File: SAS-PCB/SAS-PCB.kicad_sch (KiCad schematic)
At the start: 8 parts, among them J1 Conn_SMA_RF2-04A-T-00-50-G, J1-BMP280 Conn_01x06_Pin, J2 Conn_02x20_Odd_Even, J3-GPS Conn_01x04_Socket, J4-LCD1 Conn_01x04_Socket, J5-LCD2 Conn_01x04_Socket, J6-FAN1 Conn_01x02_Pin, J7-FAN2 Conn_01x02_Pin

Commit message: schematic done
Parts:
- removed J1: Conn_SMA_RF2-04A-T-00-50-G, CONN_RF2-04A-T-00-50-G_ADM, symbol SAS-librairie_symboles:Conn_SMA_RF2-04A-T-00-50-G
- removed J5-LCD2: Conn_01x04_Socket, symbol Connector:Conn_01x04_Socket
- removed J6-FAN1, J7-FAN2: Conn_01x02_Pin, symbol Connector:Conn_01x02_Pin
- added Bouton_1, Bouton_2, Bouton_3, Bouton_4, Bouton_5, Bouton_6, Fan_1, Fan_2, J5_Batt1, RFD900x1: 691137710002, SAS-Librarie-Empreinte:bornie_2position, symbol SAS-librairie_symboles:bornier_2position
- added J4-LCD2: Conn_01x04_Socket, SAS-Librarie-Empreinte:Conn_4_pos, symbol Connector:Conn_01x04_Socket
- added R1, R2, R3, R4, R5, R6, R7, R8: 1k, SAS-Librarie-Empreinte:Resistance, symbol Device:R
- J1-BMP280: footprint (none) -> SAS-Librarie-Empreinte:Conn_6_pos
- J2: footprint (none) -> Connector_PinSocket_2.54mm:PinSocket_2x20_P2.54mm_Vertical
- J3-GPS1: renamed from J3-GPS; footprint (none) -> SAS-Librarie-Empreinte:Conn_4_pos
- J4-LCD1: footprint (none) -> SAS-Librarie-Empreinte:Conn_4_pos
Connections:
- net +5V: now also J4-LCD1.2 (Pin_2), Fan_1.2 (5V), Fan_2.2 (5V), J4-LCD2.2 (Pin_2), J5_Batt1.2 (5V), RFD900x1.2 (5V)
- net GND: now also J1-BMP280.2 (Pin_2), J2.14 (Pin_14), J2.20 (Pin_20), J2.25 (Pin_25), J2.30 (Pin_30), J2.34 (Pin_34), J2.39 (Pin_39), J2.6 (Pin_6), J2.9 (Pin_9), J3-GPS1.4 (Pin_4), J4-LCD1.1 (Pin_1), Fan_1.1 (GND), Fan_2.1 (GND), J4-LCD2.1 (Pin_1), J5_Batt1.1 (GND), RFD900x1.1 (GND)
- net +3.3V: now reaches J3-GPS1.1 (Pin_1)
- net +3.3V: now also J1-BMP280.1 (Pin_1), J1-BMP280.5 (Pin_5), J1-BMP280.6 (Pin_6), J2.1 (Pin_1), J2.17 (Pin_17), Bouton_1.2 (5V), Bouton_2.2 (5V), Bouton_3.2 (5V), Bouton_4.2 (5V), Bouton_5.2 (5V), Bouton_6.2 (5V), R7.2, R8.2
- net TXD: now reaches J3-GPS1.2 (Pin_2)
- net TXD: now also J2.8 (Pin_8)
- net RXD: now reaches J3-GPS1.3 (Pin_3)
- net RXD: now also J2.10 (Pin_10)
- net Bouton_1: now reaches J2.27 (Pin_27)
- net Bouton_1: now also R1.2
- net Bouton_2: now reaches J2.29 (Pin_29)
- net Bouton_2: now also R2.2
- net SDA: now reaches J2.3 (Pin_3)
- net SDA: now also J1-BMP280.4 (Pin_4), J4-LCD1.3 (Pin_3), J4-LCD2.3 (Pin_3), R7.1
- net Bouton_3: now reaches J2.31 (Pin_31)
- net Bouton_3: now also R3.1
- net Bouton_4: now reaches J2.33 (Pin_33)
- net Bouton_4: now also R4.1
- net Bouton_5: now reaches J2.35 (Pin_35)
- net Bouton_5: now also R5.1
- net Bouton_6: now reaches J2.37 (Pin_37)
- net Bouton_6: now also R6.1
- net SCL: now reaches J2.5 (Pin_5)
- net SCL: now also J1-BMP280.3 (Pin_3), J4-LCD1.4 (Pin_4), J4-LCD2.4 (Pin_4), R8.1
- new net: Bouton_6.1 (GND), R6.2
- new net: Bouton_5.1 (GND), R5.2
- new net: Bouton_2.1 (GND), R2.1
- new net: Bouton_1.1 (GND), R1.1
- new net: Bouton_4.1 (GND), R4.2
- new net: Bouton_3.1 (GND), R3.2
- no-connect marks 0 -> 2
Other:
- moved on the sheet: J1-BMP280, J4-LCD1

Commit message: Rooting terminé
Reste à refaire les mounting holes et enlever les bouttes de cuivre trop mince.
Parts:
- removed Fan_1, Fan_2: 691137710002, SAS-Librarie-Empreinte:bornie_2position, symbol SAS-librairie_symboles:bornier_2position
- added J8-Fan1, J9-Fan2: Conn_01x04_Socket, SAS-Librarie-Empreinte:Conn_4_pos, symbol Connector:Conn_01x04_Socket
- J4-BMP280: renamed from J1-BMP280; footprint SAS-Librarie-Empreinte:Conn_6_pos -> SAS-Librarie-Empreinte:Header-BMP280
- J5-GPS1: renamed from J3-GPS1; footprint SAS-Librarie-Empreinte:Conn_4_pos -> SAS-Librarie-Empreinte:conn-GPS
- renumbered J5_Batt1 to J1_Batt1, J4-LCD1 to J2-LCD1, J4-LCD2 to J3-LCD2, J2 to J6-cable-plat1, RFD900x1 to J7-RFD900x1
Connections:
- net +5V: now also J8-Fan1.2 (Pin_2), J9-Fan2.2 (Pin_2)
- net GND: now also J8-Fan1.1 (Pin_1), J9-Fan2.1 (Pin_1)
- net Fan1_PWM: now reaches J6-cable-plat1.12 (Pin_12)
- net Fan1_PWM: now also J8-Fan1.4 (Pin_4)
- net Fan2_PWM: now reaches J6-cable-plat1.13 (Pin_13)
- net Fan2_PWM: now also J9-Fan2.4 (Pin_4)
- net Fan1_RPM: now reaches J6-cable-plat1.22 (Pin_22)
- net Fan1_RPM: now also J8-Fan1.3 (Pin_3)
- net Fan2_RPM: now reaches J6-cable-plat1.24 (Pin_24)
- net Fan2_RPM: now also J9-Fan2.3 (Pin_3)
- no-connect marks 2 -> 16
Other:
- note added: "BMP280-breakout"
- note added: "Battery input"
- note added: "Boutons"
- note added: "GPS Breakout"
- note added: "LCD I2C bus input"
- note added: "RFD900x Power"
- note added: "Raspberry Pi4 IO"
- moved on the sheet: Bouton_1, Bouton_2, Bouton_3, Bouton_4, Bouton_5, Bouton_6, J1_Batt1, J2-LCD1, J3-LCD2, J4-BMP280, J5-GPS1, J6-cable-plat1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

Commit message: Header Fix
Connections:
- net Bouton_1: now also J6-cable-plat1.11 (Pin_11); no longer J6-cable-plat1.27 (Pin_27)
- net Bouton_2: now also J6-cable-plat1.13 (Pin_13); no longer J6-cable-plat1.29 (Pin_29)
- net Bouton_3: now also J6-cable-plat1.15 (Pin_15); no longer J6-cable-plat1.31 (Pin_31)
- net Bouton_4: now also J6-cable-plat1.29 (Pin_29); no longer J6-cable-plat1.33 (Pin_33)
- net Bouton_5: now also J6-cable-plat1.31 (Pin_31); no longer J6-cable-plat1.35 (Pin_35)
- net Fan1_PWM: now also J6-cable-plat1.32 (Pin_32); no longer J6-cable-plat1.12 (Pin_12)
- net Fan1_RPM: now also J6-cable-plat1.16 (Pin_16); no longer J6-cable-plat1.22 (Pin_22)
- net Fan2_PWM: now also J6-cable-plat1.33 (Pin_33); no longer J6-cable-plat1.13 (Pin_13)
- net Fan2_RPM: now also J6-cable-plat1.18 (Pin_18); no longer J6-cable-plat1.24 (Pin_24)
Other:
- note added: "https://protostack.com.au/wp-content/uploads/study_refurb_05.jpg"
- moved on the sheet: Bouton_1, Bouton_2, Bouton_3, Bouton_4, Bouton_5, Bouton_6, J2-LCD1, J3-LCD2, J4-BMP280, J5-GPS1, J6-cable-plat1, J7-RFD900x1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

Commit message: u1
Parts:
- J1_Batt1, J7-RFD900x1: footprint SAS-Librarie-Empreinte:bornie_2position -> SAS-Librarie-Empreinte:AMASS_XT30U-F_1x02_P5.0mm_Vertical
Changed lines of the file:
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@@
 			)
 		)
-		(property "Footprint" "SAS-Librarie-Empreinte:bornie_2position"
+		(property "Footprint" "SAS-Librarie-Empreinte:AMASS_XT30U-F_1x02_P5.0mm_Vertical"
 			(at 152.4 111.76 0)
 			(effects
@@
 			)
 		)
-		(property "Footprint" "SAS-Librarie-Empreinte:bornie_2position"
+		(property "Footprint" "SAS-Librarie-Empreinte:AMASS_XT30U-F_1x02_P5.0mm_Vertical"
 			(at 27.94 29.21 0)
 			(effects

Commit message: U2
trial 2
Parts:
- added J10-FTDI1: Conn_01x06, SAS-Librarie-Empreinte:Conn_6_pos, symbol Connector_Generic:Conn_01x06
- added J11-Conn_RFD900: Conn_01x08, SAS-Librarie-Empreinte:Conn_8_pos, symbol Connector_Generic:Conn_01x08
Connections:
- net +5V: now also J10-FTDI1.3 (Pin_3), J11-Conn_RFD900.3 (Pin_3)
- net GND: now also J10-FTDI1.1 (Pin_1), J11-Conn_RFD900.1 (Pin_1)
- new net RFD_CTS: J10-FTDI1.2 (Pin_2), J11-Conn_RFD900.2 (Pin_2)
- new net RFD_RTS: J10-FTDI1.6 (Pin_6), J11-Conn_RFD900.6 (Pin_6)
- new net RFD_RX: J10-FTDI1.5 (Pin_5), J11-Conn_RFD900.4 (Pin_4)
- new net RFD_TX: J10-FTDI1.4 (Pin_4), J11-Conn_RFD900.5 (Pin_5)
- no-connect marks 16 -> 18
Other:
- note added: "FTDI connector"
- note added: "RFD900x connection"

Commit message: Version_a_amiliorer
pas tant fonctionnel
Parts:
- removed J11-Conn_RFD900: Conn_01x08, SAS-Librarie-Empreinte:Conn_8_pos, symbol Connector_Generic:Conn_01x08
- added J10-FTDI2: Conn_01x06, SAS-Librarie-Empreinte:Conn_6_pos, symbol Connector_Generic:Conn_01x06
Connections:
- net +5V: now also J10-FTDI2.3 (Pin_3); no longer J10-FTDI1.3 (Pin_3)
- net Fan1_RPM: now also J6-cable-plat1.18 (Pin_18); no longer J6-cable-plat1.16 (Pin_16)
- net Fan2_RPM: now also J6-cable-plat1.16 (Pin_16); no longer J6-cable-plat1.18 (Pin_18)
- net GND: now also J10-FTDI2.1 (Pin_1)
- net RFD_CTS: now also J10-FTDI2.2 (Pin_2)
- net RFD_RTS: now also J10-FTDI2.6 (Pin_6)
- net RFD_RX: now also J10-FTDI1.4 (Pin_4), J10-FTDI2.4 (Pin_4); no longer J10-FTDI1.5 (Pin_5)
- net RFD_TX: now also J10-FTDI1.5 (Pin_5), J10-FTDI2.5 (Pin_5); no longer J10-FTDI1.4 (Pin_4)
- no-connect marks 18 -> 17

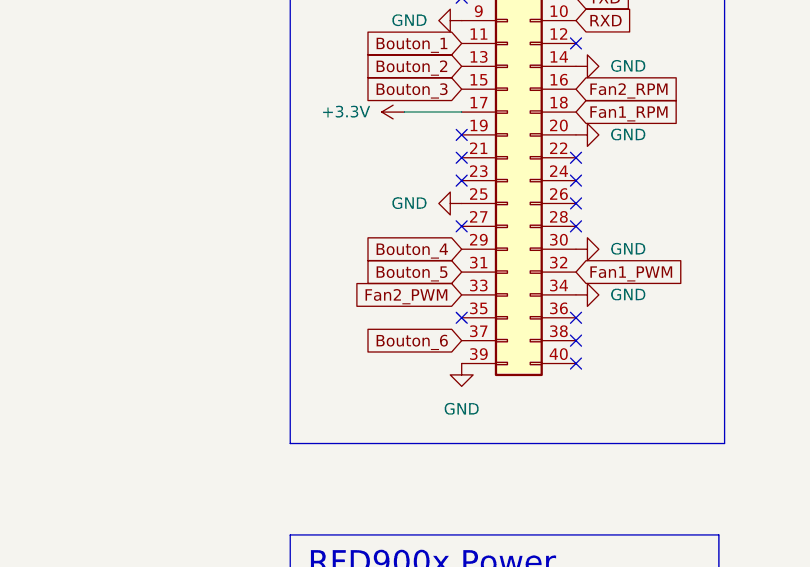
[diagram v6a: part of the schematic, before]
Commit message: Version_préliminaire
version préliminaire: fil jumper nécessaire pour certaines connections(moins de 5)
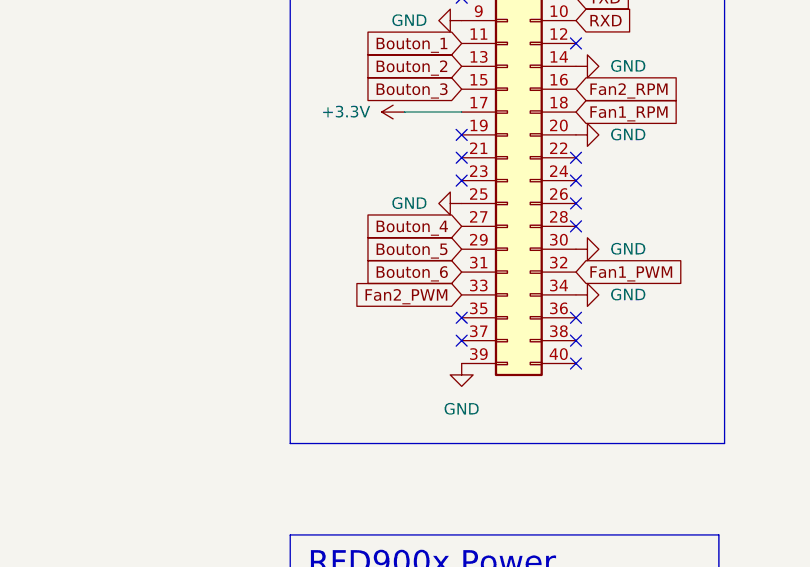
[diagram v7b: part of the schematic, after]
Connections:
- net Bouton_4: now also J6-cable-plat1.27 (Pin_27); no longer J6-cable-plat1.29 (Pin_29)
- net Bouton_5: now also J6-cable-plat1.29 (Pin_29); no longer J6-cable-plat1.31 (Pin_31)
- net Bouton_6: now also J6-cable-plat1.31 (Pin_31); no longer J6-cable-plat1.37 (Pin_37)
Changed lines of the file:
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@@
+	)
+	(no_connect
+		(at 146.05 77.47)
 	)
 	(no_connect
@@
 	(no_connect
 		(at 146.05 39.37)
-	)
-	(no_connect
-		(at 146.05 64.77)
 	)
 	(no_connect
@@
 		)
 	)
+	(global_label "Bouton_6"
+		(shape input)
+		(at 146.05 69.85 180)
+		(fields_autoplaced yes)
+		(effects
+			(font
+				(size 1.27 1.27)
+			)
+			(justify right)
+		)
+		(property "Intersheetrefs" "${INTERSHEET_REFS}"
+			(at 134.296 69.85 0)
+			(effects
+				(font
+					(size 1.27 1.27)
+				)
+				(justify right)
+				(hide yes)
+			)
+		)
+	)
 	(global_label "RFD_RX"
 		(shape input)
@@
 		)
 	)
+	(global_label "Bouton_5"
+		(shape input)
+		(at 146.05 67.31 180)
+		(fields_autoplaced yes)
+		(effects
+			(font
+				(size 1.27 1.27)
+			)
+			(justify right)
+		)
+		(property "Intersheetrefs" "${INTERSHEET_REFS}"
+			(at 134.296 67.31 0)
+			(effects
+				(font
+					(size 1.27 1.27)
+				)
+				(justify right)
+				(hide yes)
+			)
+		)
+	)
 	(global_label "SCL"
 		(shape input)
@@
 		)
 	)
-	(global_label "Bouton_6"
-		(shape input)
-		(at 146.05 77.47 180)
-		(fields_autoplaced yes)
-		(effects
-			(font
-				(size 1.27 1.27)
-			)
-			(justify right)
-		)
-		(property "Intersheetrefs" "${INTERSHEET_REFS}"
-			(at 134.296 77.47 0)
+	(global_label "RFD_RTS"
+		(shape input)
+		(at 44.45 184.15 180)
+		(fields_autoplaced yes)
+		(effects
+			(font
+				(size 1.27 1.27)
+			)
+			(justify right)
+		)
+		(property "Intersheetrefs" "${INTERSHEET_REFS}"
+			(at 33.4215 184.15 0)
 			(effects
 				(font
@@
 	(global_label "Bouton_4"
 		(shape input)
-		(at 146.05 67.31 180)
-		(fields_autoplaced yes)
-		(effects
-			(font
-				(size 1.27 1.27)
-			)
-			(justify right)
-		)
-		(property "Intersheetrefs" "${INTERSHEET_REFS}"
-			(at 134.296 67.31 0)
-			(effects
-				(font
-					(size 1.27 1.27)
-				)
-				(justify right)
-				(hide yes)
-			)
-		)
-	)
-	(global_label "RFD_RTS"
-		(shape input)
-		(at 44.45 184.15 180)
-		(fields_autoplaced yes)
-		(effects
-			(font
-				(size 1.27 1.27)
-			)
-			(justify right)
-		)
-		(property "Intersheetrefs" "${INTERSHEET_REFS}"
-			(at 33.4215 184.15 0)
+		(at 146.05 64.77 180)
+		(fields_autoplaced yes)
+		(effects
+			(font
+				(size 1.27 1.27)
+			)
+			(justify right)
+		)
+		(property "Intersheetrefs" "${INTERSHEET_REFS}"
+			(at 134.296 64.77 0)
 			(effects
 				(font
@@
 			(effects
 				(font
-					(size 1.27 1.27)
-				)
-				(justify right)
-				(hide yes)
-			)
-		)
-	)
-	(global_label "Bouton_5"
-		(shape input)
-		(at 146.05 69.85 180)
-		(fields_autoplaced yes)
-		(effects
-			(font
-				(size 1.27 1.27)
-			)
-			(justify right)
-		)
-		(property "Intersheetrefs" "${INTERSHEET_REFS}"
-			(at 134.296 69.85 0)
-			(effects
-				(font

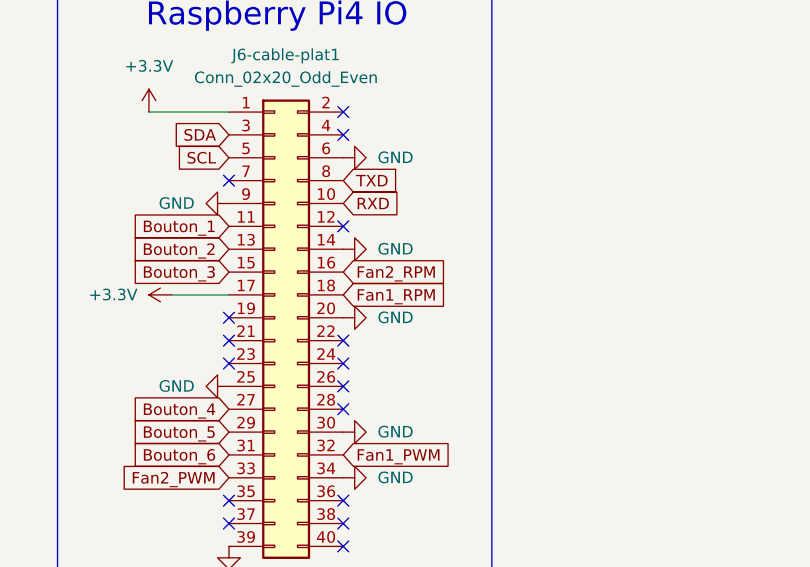
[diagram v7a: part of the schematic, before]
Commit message: Version_presque_fini
Trace fini avec via, augmentation de l'ecriture.  Il reste seulement les power plane pour 3.3V et 5V.
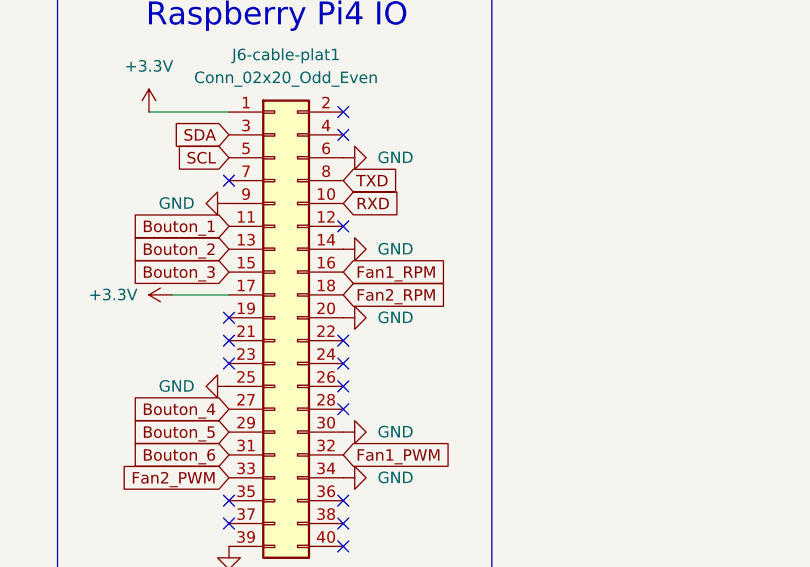
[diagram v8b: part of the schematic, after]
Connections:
- net Fan1_RPM: now also J6-cable-plat1.16 (Pin_16); no longer J6-cable-plat1.18 (Pin_18)
- net Fan2_RPM: now also J6-cable-plat1.18 (Pin_18); no longer J6-cable-plat1.16 (Pin_16)
